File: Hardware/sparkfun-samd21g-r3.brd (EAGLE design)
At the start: 57.1 x 53.3 mm, 60 parts, among them Q1 2.5A/30V, Q2 2N7002PW, U1 MCP73831, U2 74AHC1G125, U3 MIC5219 3.3V, U4 ATSAMD21G-A, Y1 32.768kHz

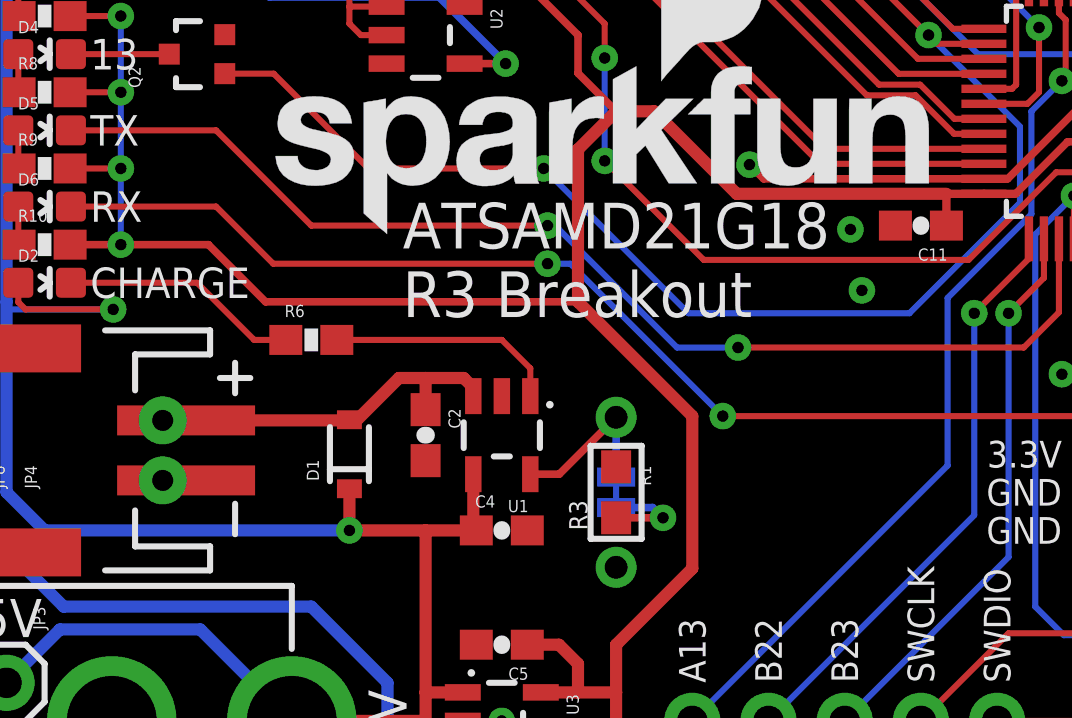
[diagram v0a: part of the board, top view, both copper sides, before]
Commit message: Renaming files and board name silk.
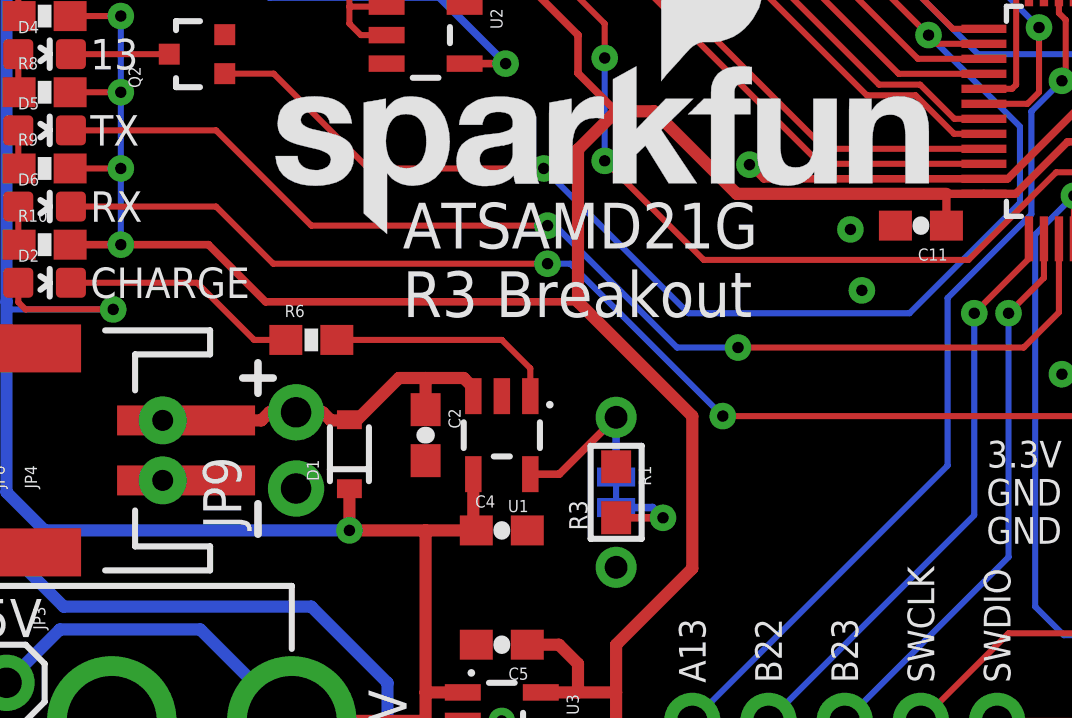
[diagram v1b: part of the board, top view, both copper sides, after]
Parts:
- added JP9: (no value), SparkFun-Connectors:1X02_NO_SILK
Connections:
- net GND: now also JP9.1
- net VBAT: now also JP9.2
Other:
- board text added: "ATSAMD21G R3 Breakout"
- board text removed: "ATSAMD21G18 R3 Breakout"
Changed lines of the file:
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@@
 <text x="4.064" y="29.845" size="1.016" layer="21" font="vector" ratio="15" align="center-left">TX</text>
 <text x="4.064" y="27.305" size="1.016" layer="21" font="vector" ratio="15" align="center-left">RX</text>
-<text x="14.478" y="27.432" size="1.524" layer="21" font="vector" ratio="15" align="top-left">ATSAMD21G18
+<text x="14.478" y="27.432" size="1.524" layer="21" font="vector" ratio="15" align="top-left">ATSAMD21G
 R3 Breakout</text>
 <text x="21.59" y="3.81" size="1.27" layer="21" font="vector" ratio="15" rot="R90" align="center-left">!RESET!</text>
@@
 <text x="40.005" y="13.97" size="0.889" layer="21" font="vector" ratio="15" align="center-left">!RESET!</text>
 <text x="39.878" y="13.97" size="0.889" layer="22" font="vector" ratio="15" rot="MR180" align="center-left">!RESET!</text>
-<text x="30.353" y="29.845" size="1.778" layer="22" font="vector" ratio="15" rot="MR45" align="top-center">ATSAMD21G18
+<text x="30.353" y="29.845" size="1.778" layer="22" font="vector" ratio="15" rot="MR45" align="top-center">ATSAMD21G
 R3 Breakout</text>
 <dimension x1="0" y1="0" x2="57.15" y2="5.08" x3="28.575" y3="-12.7" textsize="1.27" textratio="15" layer="47" dtype="horizontal" unit="inch"/>
@@
 <dimension x1="0" y1="0" x2="54.61" y2="35.56" x3="27.305" y3="-7.62" textsize="1.27" textratio="15" layer="47" dtype="horizontal" unit="inch"/>
 <text x="34.29" y="-8.89" size="1.778" layer="51" font="vector" ratio="15">Jim Lindblom</text>
-<wire x1="8.89" y1="22.098" x2="8.89" y2="21.082" width="0.2032" layer="21"/>
-<wire x1="8.89" y1="17.399" x2="8.89" y2="16.383" width="0.2032" layer="21"/>
-<wire x1="8.382" y1="21.59" x2="9.398" y2="21.59" width="0.2032" layer="21"/>
-<wire x1="6.477" y1="22.479" x2="6.477" y2="21.463" width="0.2032" layer="22"/>
-<wire x1="6.985" y1="21.971" x2="5.969" y2="21.971" width="0.2032" layer="22"/>
-<wire x1="6.477" y1="17.018" x2="6.477" y2="16.002" width="0.2032" layer="22"/>
+<wire x1="9.652" y1="22.098" x2="9.652" y2="21.082" width="0.254" layer="21"/>
+<wire x1="9.652" y1="17.399" x2="9.652" y2="16.383" width="0.254" layer="21"/>
+<wire x1="9.144" y1="21.59" x2="10.16" y2="21.59" width="0.254" layer="21"/>
+<wire x1="10.922" y1="22.733" x2="10.922" y2="21.717" width="0.254" layer="22"/>
+<wire x1="11.43" y1="22.225" x2="10.414" y2="22.225" width="0.254" layer="22"/>
+<wire x1="10.922" y1="16.637" x2="10.922" y2="15.621" width="0.254" layer="22"/>
 <wire x1="51.816" y1="31.75" x2="52.578" y2="31.75" width="0.2032" layer="21"/>
 </plain>
@@
 </element>
 <element name="JP8" library="SparkFun-Connectors" package="JST-2-PTH-NS" value="" x="6.477" y="19.177" rot="R90"/>
+<element name="JP9" library="SparkFun-Connectors" package="1X02_NO_SILK" value="" x="10.922" y="17.907" rot="R90"/>
 </elements>
 <signals>
@@
 <wire x1="5.618" y1="39.34" x2="6.477" y2="38.481" width="0.4064" layer="1"/>
 <contactref element="JP8" pad="1"/>
+<contactref element="JP9" pad="1"/>
 </signal>
 <signal name="3.3V">
@@
 <contactref element="D1" pad="A"/>
 <contactref element="JP4" pad="2"/>
-<wire x1="7.256" y1="20.177" x2="12.677" y2="20.177" width="0.4064" layer="1"/>
 <wire x1="12.677" y1="20.177" x2="12.7" y2="20.2" width="0.4064" layer="1"/>
 <wire x1="12.7" y1="20.2" x2="12.961" y2="20.2" width="0.4064" layer="1"/>
@@
 <contactref element="JP8" pad="2"/>
 <wire x1="6.477" y1="20.177" x2="7.256" y2="20.177" width="0.2032" layer="1"/>
+<contactref element="JP9" pad="2"/>
+<wire x1="10.922" y1="20.447" x2="10.033" y2="20.447" width="0.4064" layer="1"/>
+<wire x1="10.033" y1="20.447" x2="9.763" y2="20.177" width="0.4064" layer="1"/>
+<wire x1="7.256" y1="20.177" x2="9.763" y2="20.177" width="0.4064" layer="1"/>
+<wire x1="10.922" y1="20.447" x2="11.811" y2="20.447" width="0.4064" layer="1"/>
+<wire x1="12.677" y1="20.177" x2="12.081" y2="20.177" width="0.4064" layer="1"/>
+<wire x1="12.081" y1="20.177" x2="11.811" y2="20.447" width="0.4064" layer="1"/>
 </signal>
 <signal name="N$13">

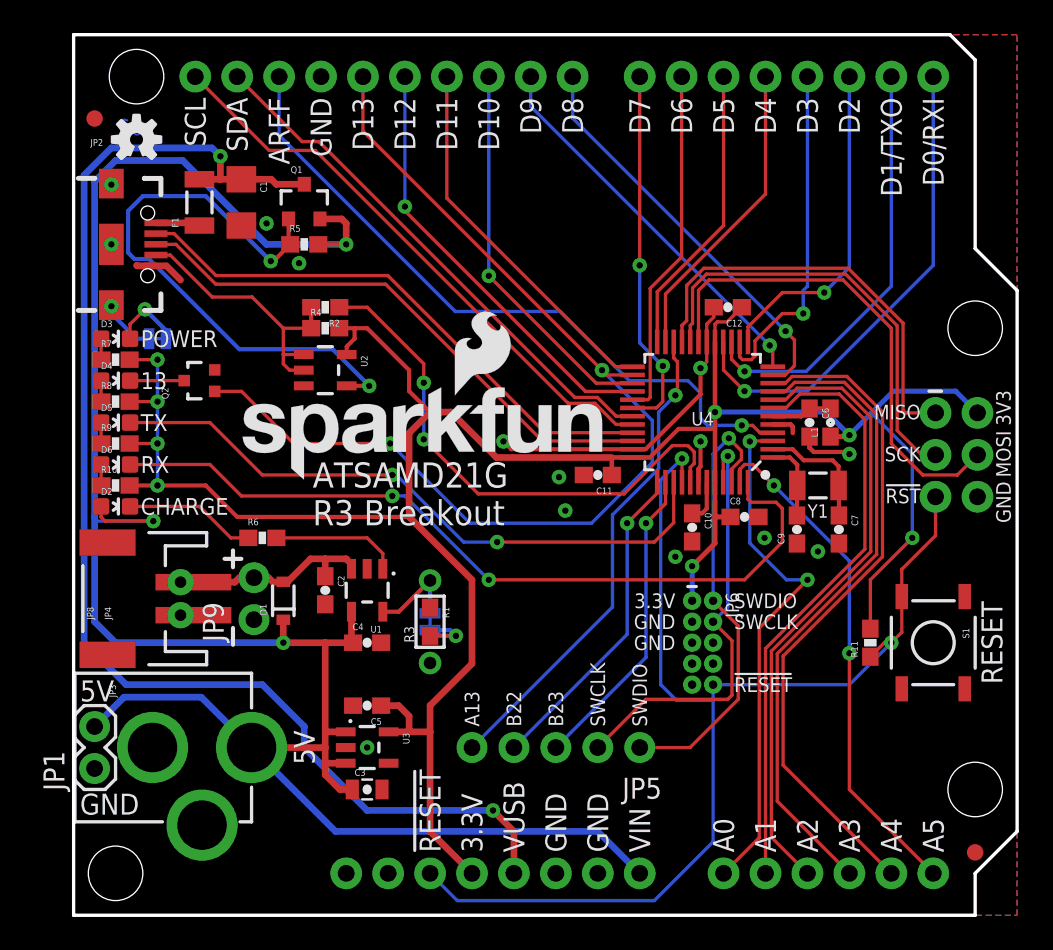
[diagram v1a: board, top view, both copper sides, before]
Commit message: Re-routing some traces to increase ground pour.
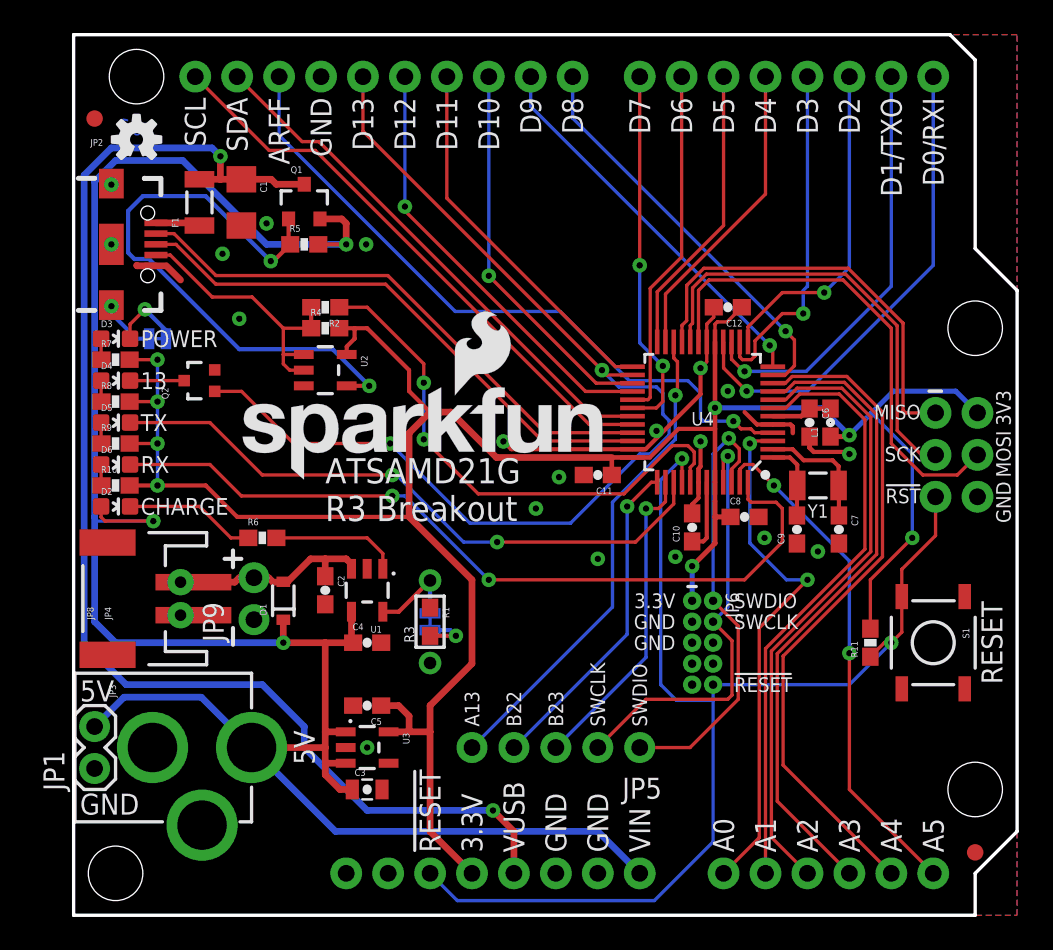
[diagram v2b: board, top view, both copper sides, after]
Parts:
- turned C10 to 90 degrees
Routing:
- net GND: track 32.3 -> 36.4 mm, vias 15 -> 20
- net D13: track 64.0 -> 65.8 mm
- net VDDCORE: track 2.60 -> 4.35 mm
- net TX_LED: track 38.9 -> 38.2 mm

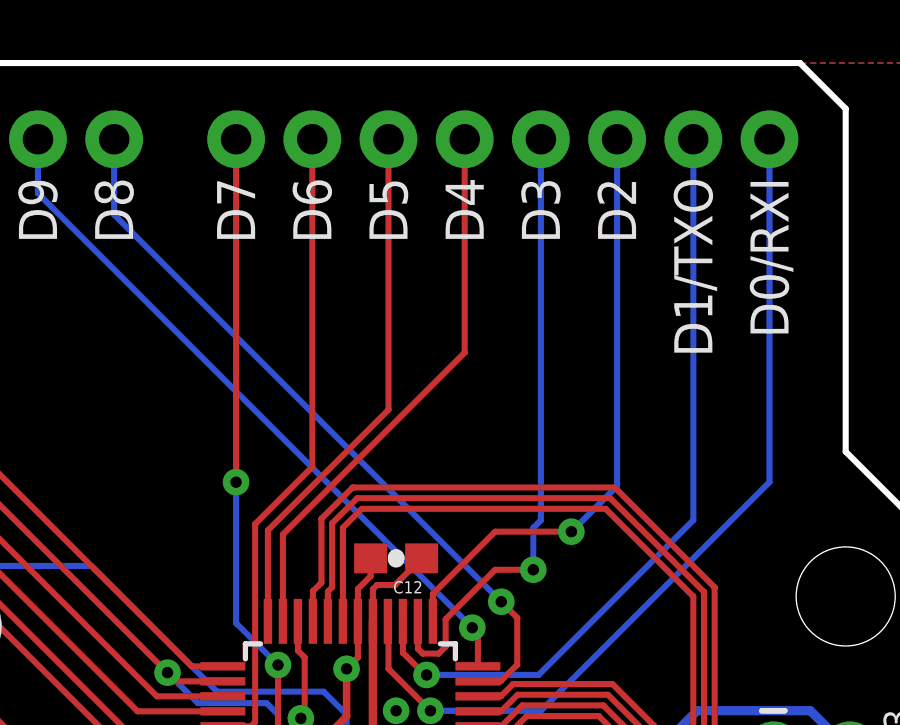
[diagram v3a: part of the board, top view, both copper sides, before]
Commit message: Swapping D2 and D4.
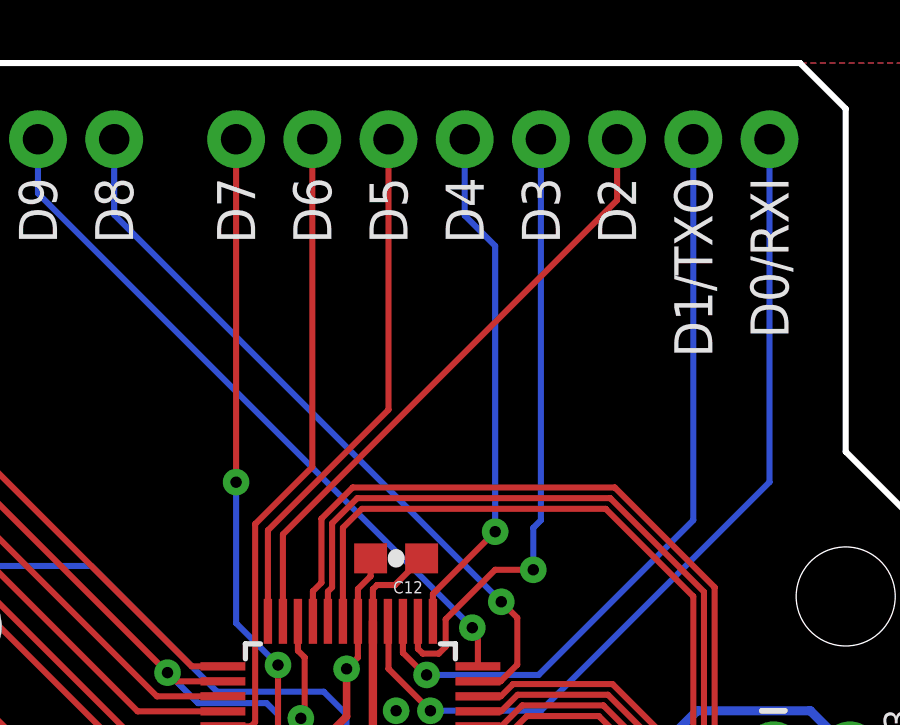
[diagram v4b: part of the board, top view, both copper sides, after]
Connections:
- net D2: now also U4.23; no longer U4.13
- net D4: now also U4.13; no longer U4.23
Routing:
- net D4: track 18.6 -> 17.4 mm, vias 0 -> 1
- net D2: track 20.1 -> 20.7 mm, vias 1 -> 0
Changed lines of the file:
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@@
 <layer number="47" name="Measures" color="7" fill="1" visible="no" active="yes"/>
 <layer number="48" name="Document" color="7" fill="1" visible="no" active="yes"/>
-<layer number="49" name="Reference" color="7" fill="1" visible="yes" active="yes"/>
+<layer number="49" name="Reference" color="7" fill="1" visible="no" active="yes"/>
 <layer number="50" name="dxf" color="7" fill="1" visible="no" active="no"/>
 <layer number="51" name="tDocu" color="6" fill="1" visible="yes" active="yes"/>
@@
 <wire x1="44.45" y1="31.75" x2="52.07" y2="39.37" width="0.2032" layer="16"/>
 </signal>
-<signal name="D2">
+<signal name="D4">
 <contactref element="U4" pad="13"/>
-<contactref element="JP7" pad="D2"/>
 <wire x1="40.85" y1="34.73" x2="40.85" y2="35.643" width="0.2032" layer="1"/>
-<via x="45.466" y="37.719" extent="1-16" drill="0.381"/>
+<via x="42.926" y="37.719" extent="1-16" drill="0.381"/>
 <wire x1="40.85" y1="35.643" x2="42.926" y2="37.719" width="0.2032" layer="1"/>
-<wire x1="42.926" y1="37.719" x2="45.466" y2="37.719" width="0.2032" layer="1"/>
-<wire x1="45.466" y1="37.719" x2="46.99" y2="39.243" width="0.2032" layer="16"/>
-<wire x1="46.99" y1="39.243" x2="46.99" y2="50.8" width="0.2032" layer="16"/>
+<contactref element="JP7" pad="D4"/>
+<wire x1="42.926" y1="37.719" x2="42.926" y2="47.244" width="0.2032" layer="16"/>
+<wire x1="42.926" y1="47.244" x2="41.91" y2="48.26" width="0.2032" layer="16"/>
+<wire x1="41.91" y1="48.26" x2="41.91" y2="50.8" width="0.2032" layer="16"/>
 </signal>
 <signal name="D3">
@@
 <wire x1="42.926" y1="36.449" x2="41.275" y2="34.798" width="0.2032" layer="1"/>
 </signal>
-<signal name="D4">
+<signal name="D2">
 <contactref element="U4" pad="23"/>
-<contactref element="JP7" pad="D4"/>
-<wire x1="35.85" y1="37.628" x2="41.91" y2="43.688" width="0.2032" layer="1"/>
-<wire x1="41.91" y1="43.688" x2="41.91" y2="50.8" width="0.2032" layer="1"/>
+<wire x1="35.85" y1="37.628" x2="46.99" y2="48.768" width="0.2032" layer="1"/>
 <wire x1="35.85" y1="34.73" x2="35.85" y2="37.628" width="0.2032" layer="1"/>
+<contactref element="JP7" pad="D2"/>
+<wire x1="46.99" y1="48.768" x2="46.99" y2="50.8" width="0.2032" layer="1"/>
 </signal>
 <signal name="D5">

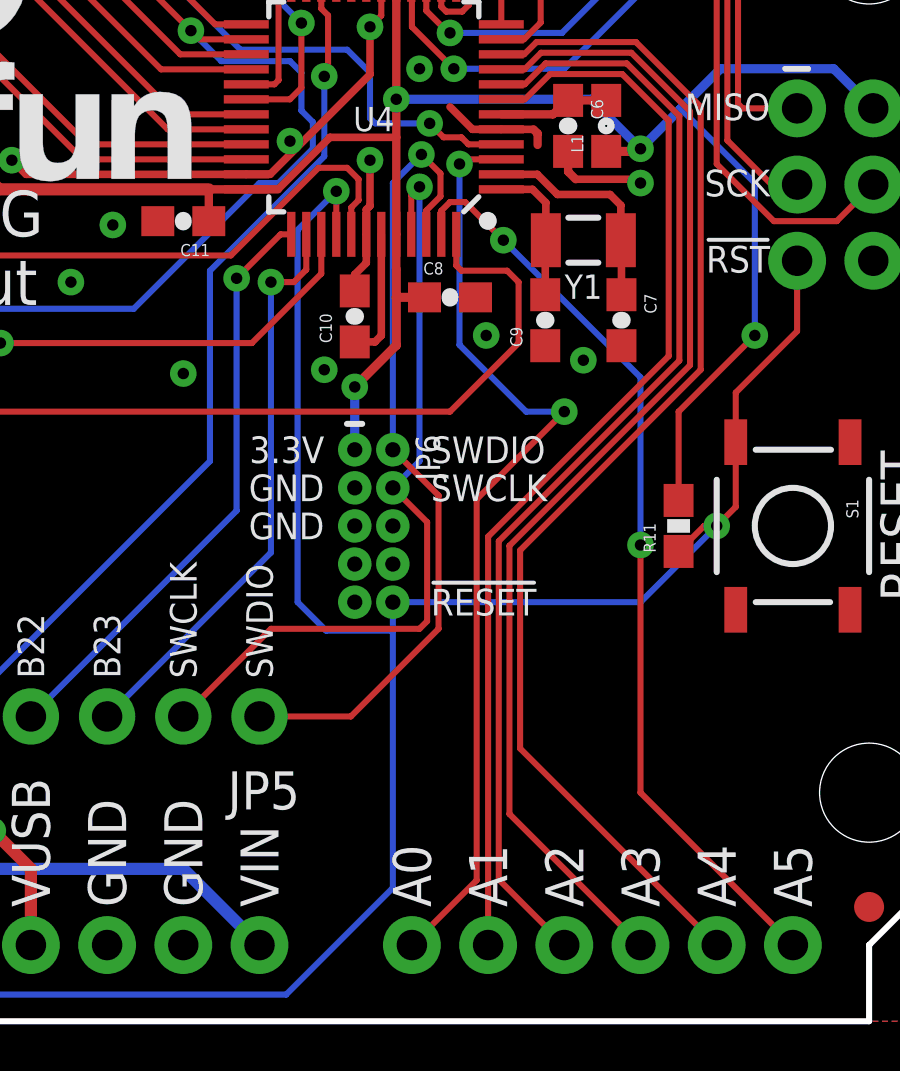
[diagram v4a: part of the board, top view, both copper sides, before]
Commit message: Moving Cortex-M0 programming header down 0.025"
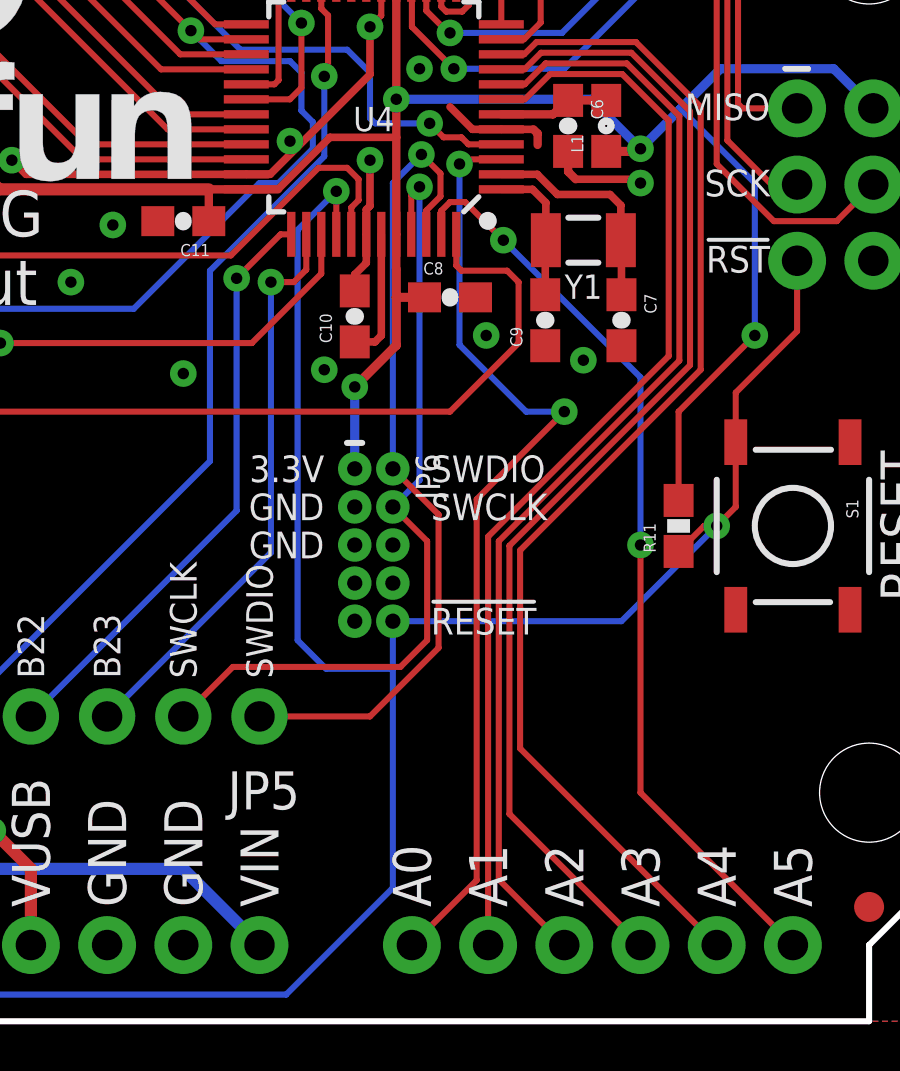
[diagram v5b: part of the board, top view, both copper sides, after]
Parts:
- moved JP6 0.64 mm to (38.1, 15.9)
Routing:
- net !RESET: track 71.5 -> 72.4 mm
- net 3.3V: track 153.2 -> 153.8 mm
